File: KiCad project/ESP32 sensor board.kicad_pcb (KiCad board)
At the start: 2 copper layers, 50 parts, among them J1 USB_C_Receptacle, J3 JST_2mm_LiPo, U1 MCP73871, U2 AMS1117-3.3, U3 ESP32-C3-WROOM-02-H4, U4 CP2102N-Axx-xQFN20

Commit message: Fixed lots of bugs.
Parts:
- removed the C10 at (105.5, 117.2)
- removed the C3 at (146.6, 117.8)
- removed the C4 at (146.6, 120.8)
- removed the C6 at (146.6, 126.9)
- removed the C9 at (146.6, 132.9)
- removed the D1 at (164.0, 119.7)
- removed D10: Red, SparkFun-LED:LED_0603_1608Metric
- removed the D2 at (163.4, 134.9)
- removed the D6 at (102.5, 135.4)
- removed D7: PESD5V0S1UL_315, Footprints:DIO_PESD5V0S1UL_315
- removed the R13 at (84.0, 135.7)
- removed the R2 at (157.2, 60.3)
- removed the R9 at (166.1, 57.4)
- added C1: 0.1u, Project_Library:C_0805_2012Metric, F.Cu at (77.5, 118.5)
- added C11: 1u, Project_Library:C_0805_2012Metric, F.Cu at (66.1, 98.4)
- added C12: 10u, Project_Library:C_0805_2012Metric, F.Cu at (66.1, 107.5)
- added C13: 0.1u, Project_Library:C_0805_2012Metric, F.Cu at (66.1, 110.5)
- added C14: 0.1u, Project_Library:C_0805_2012Metric, F.Cu at (66.1, 104.5)
- added C15: 0.1u, Project_Library:C_0805_2012Metric, F.Cu at (80.2, 101.4)
- added C16: 100n, Project_Library:C_0805_2012Metric, F.Cu at (230.4, 89.2)
- added C17: 10n, Project_Library:C_0805_2012Metric, F.Cu at (230.4, 86.2)
- added C18: 100n, Project_Library:C_0805_2012Metric, F.Cu at (230.4, 77.1)
- added C19: 1u, Project_Library:C_0805_2012Metric, F.Cu at (230.4, 83.2)
- added C2: 0.1u, Project_Library:C_0805_2012Metric, F.Cu at (77.5, 121.5)
- added C20: 100n, Project_Library:C_0805_2012Metric, F.Cu at (230.4, 80.1)
- added C21: 0.1u, Project_Library:C_0805_2012Metric, F.Cu at (230.6, 104.1)
- added C22: 1u, Project_Library:C_0805_2012Metric, F.Cu at (71.0, 120.7)
- added C8: 0.1u, Project_Library:C_0805_2012Metric, F.Cu at (66.1, 101.4)
- added D4: Red, Project_Library:LED_0603_1608Metric, F.Cu at (193.4, 107.3)
- added J3: GSD090012SEU, Project_Library:AMPHENOL_GSD090012SEU, F.Cu at (206.6, 83.8)
- added J4: B4B-XH-AM__LF__SN_, Project_Library:JST_B4B-XH-AM__LF__SN_, F.Cu at (230.7, 72.0)
- added J5: B4B-XH-AM__LF__SN_, Project_Library:JST_B4B-XH-AM__LF__SN_, F.Cu at (235.3, 99.0)
- added J6: Conn_01x05, Project_Library:PinHeader_1x05_P2.54mm_Vertical, F.Cu at (226.1, 97.7)
- added MK1: CMC-5042PF-AC, Project_Library:CUI_CMC-5042PF-AC, F.Cu at (236.4, 79.4)
- added Q1: TEMT6000X01, Project_Library:TRANS_TEMT6000X01, F.Cu at (240.3, 86.0)
- added Q2: BC817, Project_Library:SOT-23, F.Cu at (66.3, 116.4)
- added Q3: BC817, Project_Library:SOT-23, F.Cu at (66.3, 121.0)
- added R17: 50, Project_Library:R_0201_0603Metric, F.Cu at (69.6, 97.8)
- added R19: 10K, Project_Library:R_0805_2012Metric, F.Cu at (203.9, 98.5)
- added R20: 50, Project_Library:R_0201_0603Metric, F.Cu at (69.6, 101.3)
- added R22: 50, Project_Library:R_0201_0603Metric, F.Cu at (69.6, 104.8)
- added R23: 10K, Project_Library:R_0201_0603Metric, F.Cu at (83.6, 101.3)
- added R24: 4K7, Project_Library:R_0201_0603Metric, F.Cu at (83.6, 97.8)
- added R25: 4K7, Project_Library:R_0201_0603Metric, F.Cu at (90.7, 99.3)
- added R26: 2K, Project_Library:R_0805_2012Metric, F.Cu at (225.9, 91.8)
- added R27: 1M, Project_Library:R_0805_2012Metric, F.Cu at (225.9, 86.0)
- added R28: 2K, Project_Library:R_0805_2012Metric, F.Cu at (225.9, 88.9)
- added R29: 1M, Project_Library:R_0805_2012Metric, F.Cu at (225.9, 83.0)
- added R30: 10K, Project_Library:R_0805_2012Metric, F.Cu at (225.9, 80.0)
- added R31: 100K, Project_Library:R_0805_2012Metric, F.Cu at (225.9, 77.1)
- added R32: 10K, Project_Library:R_0201_0603Metric, F.Cu at (70.0, 116.6)
- added R33: 10K, Project_Library:R_0201_0603Metric, F.Cu at (70.0, 114.8)
- added R34: 10K, Project_Library:R_0201_0603Metric, F.Cu at (70.0, 118.3)
- added SW1: SMD_6x3.5mm_h2.5mm, Project_Library:SW_PUSH_6mm, F.Cu at (198.9, 122.5)
- added SW2: SMD_6x3.5mm_h2.5mm, Project_Library:SW_PUSH_6mm, F.Cu at (198.9, 131.1)
- added U5: USBLC6-2SC6, Project_Library:SOT-23-6, F.Cu at (73.4, 99.3)
- added U6: W25Q32JVSSIQ, Project_Library:SOIC127P790X216-8N, F.Cu at (196.6, 100.5)
- added U7: BME280, Project_Library:PSON65P250X250X100-8N, F.Cu at (59.9, 99.1)
- added U8: MAX4466EXK, Project_Library:SOT65P210X110-5N, F.Cu at (80.1, 106.8)
- C10: renamed from C11; value 0.1 uF -> 0.1u; footprint Capacitor_SMD:C_0805_2012Metric -> Project_Library:C_0805_2012Metric
- C3: renamed from C1; value 10 uF -> 10u; footprint Capacitor_SMD:C_0805_2012Metric -> Project_Library:C_0805_2012Metric
- C4: renamed from C2; value 10 uF -> 10u; footprint Capacitor_SMD:C_0805_2012Metric -> Project_Library:C_0805_2012Metric
- C5: value 4.7 uF -> 0.1u; footprint Capacitor_SMD:C_0805_2012Metric -> Project_Library:C_0805_2012Metric
- C6: renamed from C7; value 1 uF -> 1u; footprint Capacitor_SMD:C_0805_2012Metric -> Project_Library:C_0805_2012Metric
- C7: renamed from C8; value 10 uF -> 10u; footprint Capacitor_SMD:C_0805_2012Metric -> Project_Library:C_0805_2012Metric
- C9: renamed from C12; value 4.7 uF -> 4.7u; footprint Capacitor_SMD:C_0805_2012Metric -> Project_Library:C_0805_2012Metric
- D1: renamed from D3; footprint SparkFun-LED:LED_0603_1608Metric -> Project_Library:LED_0603_1608Metric
- D2: renamed from D4; footprint SparkFun-LED:LED_0603_1608Metric -> Project_Library:LED_0603_1608Metric
- D3: renamed from D5; footprint SparkFun-LED:LED_0603_1608Metric -> Project_Library:LED_0603_1608Metric
- D5: renamed from D9; footprint SparkFun-LED:LED_0603_1608Metric -> Project_Library:LED_0603_1608Metric
- D6: renamed from D8; footprint SparkFun-LED:LED_0603_1608Metric -> Project_Library:LED_0603_1608Metric
- F1: footprint SparkFun-Fuse:1210 -> Project_Library:1210
- J1: footprint SparkFun-Connector:USB-C_16 -> Project_Library:USB-C_16
- J2: renamed from J3; footprint SparkFun-Connector:JST_SMD_2.0mm-2 -> Project_Library:JST_SMD_2.0mm-2
- R1: renamed from R7; value 10 KOhm -> 10K; footprint Resistor_SMD:R_0805_2012Metric -> Project_Library:R_0805_2012Metric
- R10: value 10 KOhm -> 330; footprint Resistor_SMD:R_0805_2012Metric -> Project_Library:R_0805_2012Metric
- R11: renamed from R18; value 1 KOhn -> 1K; footprint Resistor_SMD:R_0805_2012Metric -> Project_Library:R_0805_2012Metric
- R12: renamed from R14; value 22.1 KOhm -> 22K1; footprint Resistor_SMD:R_0805_2012Metric -> Project_Library:R_0805_2012Metric
- R13: renamed from R17; value 47.5 KOhm -> 47K5; footprint Resistor_SMD:R_0805_2012Metric -> Project_Library:R_0805_2012Metric
- R14: renamed from R20; value 330 Ohm -> 330; footprint Resistor_SMD:R_0805_2012Metric -> Project_Library:R_0805_2012Metric
- R15, R16: value 1 KOhn -> 50; footprint Resistor_SMD:R_0805_2012Metric -> Project_Library:R_0201_0603Metric
- R18: renamed from R19; value 330 Ohm -> 330; footprint Resistor_SMD:R_0805_2012Metric -> Project_Library:R_0805_2012Metric
- R2: renamed from R8; value 10 KOhm -> 10K; footprint Resistor_SMD:R_0805_2012Metric -> Project_Library:R_0805_2012Metric
- R21: value 330 Ohm -> 50; footprint Resistor_SMD:R_0805_2012Metric -> Project_Library:R_0201_0603Metric
- R3: renamed from R11; value 5.1 KOhm -> 5k1; footprint Resistor_SMD:R_0805_2012Metric -> Project_Library:R_0805_2012Metric
- R4: renamed from R12; value 5.1 KOhm -> 5K1; footprint Resistor_SMD:R_0805_2012Metric -> Project_Library:R_0805_2012Metric
- R5: renamed from R1; value 2 KOhm -> 2K; footprint Resistor_SMD:R_0805_2012Metric -> Project_Library:R_0805_2012Metric
- R6: renamed from R3; value 20 KOhm -> 20K; footprint Resistor_SMD:R_0805_2012Metric -> Project_Library:R_0805_2012Metric
- R7: renamed from R4; value 470 Ohm -> 470; footprint Resistor_SMD:R_0805_2012Metric -> Project_Library:R_0805_2012Metric
- R8: renamed from R5; value 470 Ohm -> 470; footprint Resistor_SMD:R_0805_2012Metric -> Project_Library:R_0805_2012Metric
- R9: renamed from R6; value 470 Ohm -> 470; footprint Resistor_SMD:R_0805_2012Metric -> Project_Library:R_0805_2012Metric
- U1: footprint Package_DFN_QFN:QFN-20-1EP_4x4mm_P0.5mm_EP2.5x2.5mm -> Project_Library:QFN-20-1EP_4x4mm_P0.5mm_EP2.5x2.5mm
- U2: footprint Package_TO_SOT_SMD:SOT-223-3_TabPin2 -> Project_Library:SOT-223-3_TabPin2
- U3: footprint Footprints:MODULE_ESP32-C3-WROOM-02-H4 -> Project_Library:MODULE_ESP32-C3-WROOM-02-H4
- U4: value CP2102N-Axx-xQFN20 -> CP2102N-A02-GQFN20; footprint Package_DFN_QFN:SiliconLabs_QFN-20-1EP_3x3mm_P0.5mm_EP1.8x1.8mm -> Project_Library:SiliconLabs_QFN-20-1EP_3x3mm_P0.5mm_EP1.8x1.8mm
- moved R10 100.6 mm to (81.9, 115.5)
- moved C5 69.7 mm to (77.5, 115.5)
- moved R21 40.0 mm to (69.6, 103.0)
- moved R15 37.9 mm to (69.6, 106.5)
- moved R16 33.3 mm to (69.6, 108.3)
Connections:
- C10 pad 1: VBUS -> 3.3V
- C3 pad 1: /+5V_USB -> +5V
- C5 pad 1: GND -> 3.3V
- C5 pad 2: /+5V_USB -> GND
- C9 pad 1: VBUS -> 3.3V
- F1 pad 1: Net-(D2-PadA) -> Net-(C1-Pad1)
- J1 pad A6: /D+ -> /USB_DN
- J1 pad A7: /D- -> /USB_DP
- J1 pad B6: /D+ -> /USB_DN
- J1 pad B7: /D- -> /USB_DP
- J1 pad S: unconnected-(J1-SHIELD-PadS) -> GND
- J1 pad VBUS: Net-(D2-PadC) -> Net-(C1-Pad1)
- R10 pad 1: Net-(U1-CE) -> GND
- R10 pad 2: /+5V_USB -> Net-(D4-K)
- R11 pad 1: VBUS -> 3.3V
- R12 pad 1: VBUS -> /+5V_USB
- R15 pad 1: Net-(U4-TXD) -> Net-(J3-CMD)
- R15 pad 2: Net-(U3-RXD) -> /ESP32-C3-02/MOSI_DI
- R16 pad 1: Net-(U4-RXD) -> Net-(J3-DAT0)
- R16 pad 2: Net-(U3-TXD) -> /ESP32-C3-02/MISO_DO
- R21 pad 1: GND -> /ESP32-C3-02/MOSI_DI
- U1 pad 1: /+5V_USB -> +5V
- U1 pad 17: Net-(U1-CE) -> /+5V_USB
- U1 pad 20: /+5V_USB -> +5V
- U1 pad 3: Net-(U1-SEL) -> GND
- U1 pad 4: Net-(U1-PROG2) -> /+5V_USB
- U2 pad 3: /+5V_USB -> +5V
- U3 pad 10: unconnected-(U3-IO10-Pad10) -> /ESP32-C3-02/CS
- U3 pad 11: Net-(U3-RXD) -> /ESP32-C3-02/TX_RX
- U3 pad 12: Net-(U3-TXD) -> /ESP32-C3-02/RX_TX
- U3 pad 13: unconnected-(U3-IO18-Pad13) -> /ESP32-C3-02/GPIO18
- U3 pad 14: unconnected-(U3-IO19-Pad14) -> /ESP32-C3-02/GPIO19
- U3 pad 15: unconnected-(U3-IO3-Pad15) -> /ESP32-C3-02/SCL
- U3 pad 16: unconnected-(U3-IO2-Pad16) -> /ESP32-C3-02/MISO_DO
- U3 pad 17: unconnected-(U3-IO1-Pad17) -> /ESP32-C3-02/PHOTO_C
- U3 pad 18: unconnected-(U3-IO0-Pad18) -> /ESP32-C3-02/CS_SD
- U3 pad 2: Net-(U3-EN) -> /ESP32-C3-02/EN
- U3 pad 3: unconnected-(U3-IO4-Pad3) -> /ESP32-C3-02/SDA
- U3 pad 4: unconnected-(U3-IO5-Pad4) -> /ESP32-C3-02/MIC_OUT
- U3 pad 5: unconnected-(U3-IO6-Pad5) -> /ESP32-C3-02/SCLK
- U3 pad 6: unconnected-(U3-IO7-Pad6) -> /ESP32-C3-02/MOSI_DI
- U3 pad 7: unconnected-(U3-IO8-Pad7) -> /ESP32-C3-02/GPIO8
- U3 pad 8: unconnected-(U3-IO9-Pad8) -> /ESP32-C3-02/BOOT
- U4 pad 15: unconnected-(U4-~{CTS}-Pad15) -> /ESP32-C3-02/DTS
- U4 pad 16: unconnected-(U4-~{RTS}-Pad16) -> /ESP32-C3-02/RTS
- U4 pad 17: Net-(U4-RXD) -> /ESP32-C3-02/RX_TX
- U4 pad 18: Net-(U4-TXD) -> /ESP32-C3-02/TX_RX
- U4 pad 4: /D+ -> Net-(U4-D+)
- U4 pad 5: /D- -> Net-(U4-D-)
- U4 pad 7: VBUS -> 3.3V

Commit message: Configured the layout editor.
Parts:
- C1, C10, C11, C12, C13, C14, C15, C16, C17, C18, C19, C2, C20, C21, C22, C3, C4, C5, C6, C7, C8, C9: footprint Project_Library:C_0805_2012Metric -> Capacitor_SMD:C_0805_2012Metric
- D1, D2, D3, D4, D5, D6: footprint Project_Library:LED_0603_1608Metric -> LED_SMD:LED_0603_1608Metric
- J6: footprint Project_Library:PinHeader_1x05_P2.54mm_Vertical -> Connector_PinHeader_2.54mm:PinHeader_1x05_P2.54mm_Vertical
- Q2, Q3: footprint Project_Library:SOT-23 -> Package_TO_SOT_SMD:SOT-23
- R1, R10, R11, R12, R13, R14, R18, R19, R2, R26, R27, R28, R29, R3, R30, R31, R4, R5, R6, R7, R8, R9: footprint Project_Library:R_0805_2012Metric -> Resistor_SMD:R_0805_2012Metric
- R15, R16, R17, R20, R21, R22, R23, R24, R25, R32, R33, R34: footprint Project_Library:R_0201_0603Metric -> Resistor_SMD:R_0805_2012Metric
- SW1, SW2: footprint Project_Library:SW_PUSH_6mm -> Button_Switch_THT:SW_PUSH_6mm
- U1: footprint Project_Library:QFN-20-1EP_4x4mm_P0.5mm_EP2.5x2.5mm -> Package_DFN_QFN:QFN-20-1EP_4x4mm_P0.5mm_EP2.5x2.5mm
- U2: footprint Project_Library:SOT-223-3_TabPin2 -> Package_TO_SOT_SMD:SOT-223-3_TabPin2
- U4: footprint Project_Library:SiliconLabs_QFN-20-1EP_3x3mm_P0.5mm_EP1.8x1.8mm -> Package_DFN_QFN:SiliconLabs_QFN-20-1EP_3x3mm_P0.5mm_EP1.8x1.8mm
- U5: footprint Project_Library:SOT-23-6 -> Package_TO_SOT_SMD:SOT-23-6

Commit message: Completed draft layout.
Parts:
- removed J4: B4B-XH-AM__LF__SN_, Project_Library:JST_B4B-XH-AM__LF__SN_
- removed R4: 5K1, Resistor_SMD:R_0805_2012Metric
- moved Q3 123.4 mm to (184.0, 83.8)
- moved R32 121.4 mm to (191.2, 110.8)
- moved C22 120.6 mm to (191.5, 115.2), turned to 180 degrees
- moved Q2 118.3 mm to (184.5, 111.0)
- moved Q1 115.7 mm to (125.0, 76.2)
- moved R34 114.1 mm to (178.5, 83.0)
- moved C8 112.5 mm to (178.2, 92.5)
- moved R20 108.8 mm to (178.2, 97.2)
- moved R21 108.7 mm to (178.2, 101.0)
- moved R22 108.7 mm to (178.2, 104.8)
- moved R33 108.1 mm to (178.0, 109.5)
- moved C14 103.8 mm to (169.0, 90.5), turned to 180 degrees
- moved D4 99.7 mm to (94.2, 118.0), turned to 180 degrees
- moved U3 88.3 mm to (192.7, 96.6), turned to -90 degrees
- moved R8 84.8 mm to (99.2, 114.8), turned to 180 degrees
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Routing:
- net /USB_DN: track 0.00 -> 3.54 mm
- net /USB_DP: track 0.00 -> 3.33 mm
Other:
- copper layers 2 -> 4

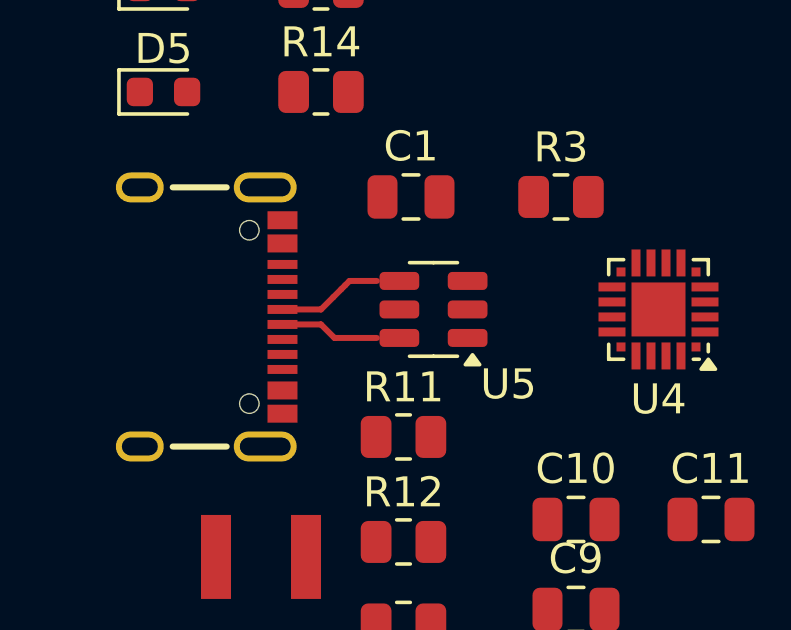
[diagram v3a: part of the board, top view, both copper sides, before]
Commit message: Experimenting with lenght tuning of the USB data tracks.
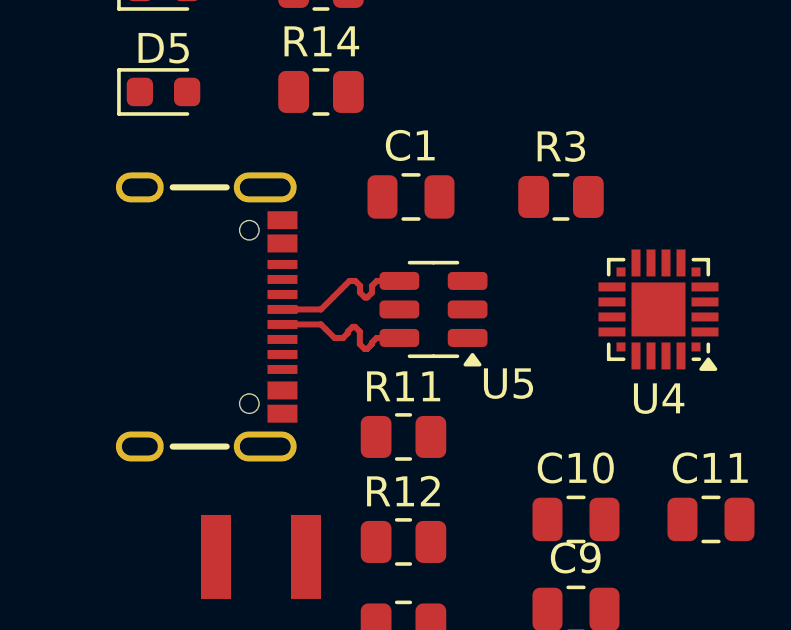
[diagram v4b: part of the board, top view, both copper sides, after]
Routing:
- net /USB_DP: track 3.33 -> 5.00 mm
- net /USB_DN: track 3.54 -> 5.01 mm

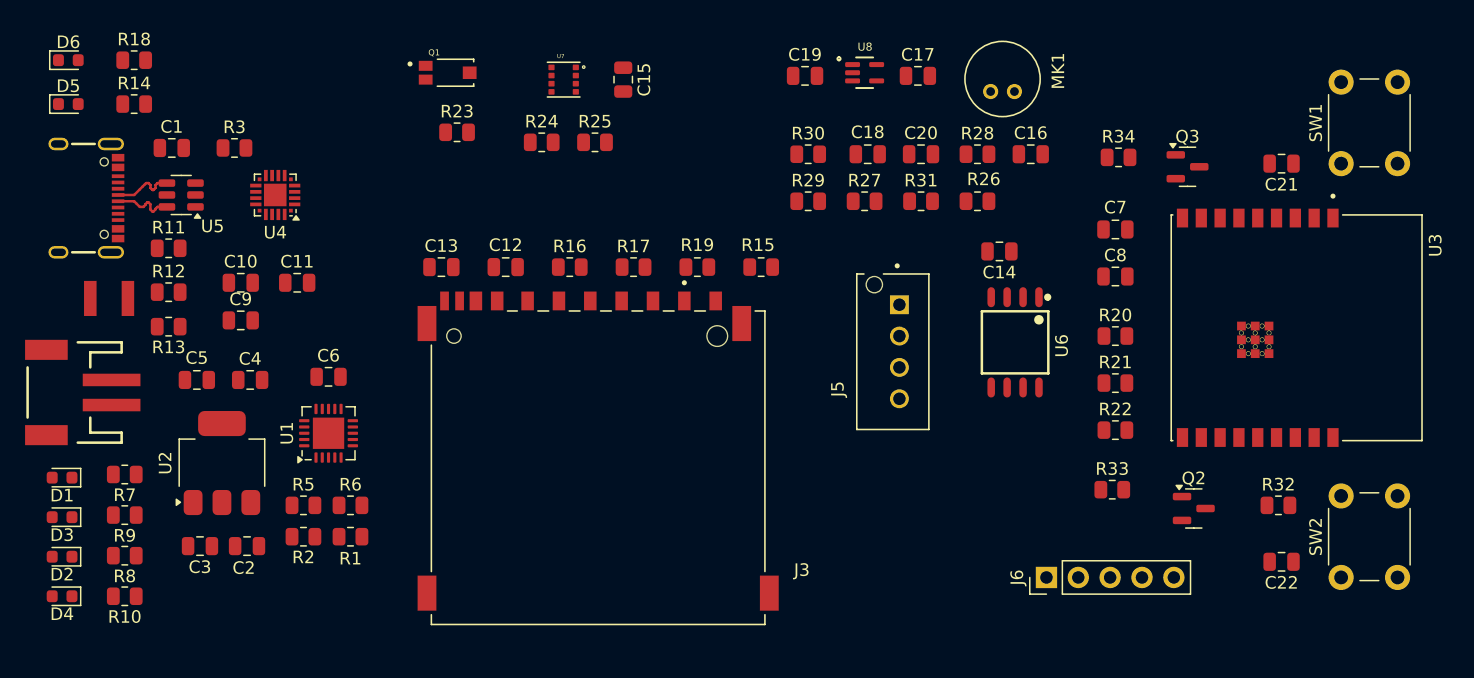
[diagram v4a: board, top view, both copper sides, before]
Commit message: Autorouting experiment. Layout is incomplete.
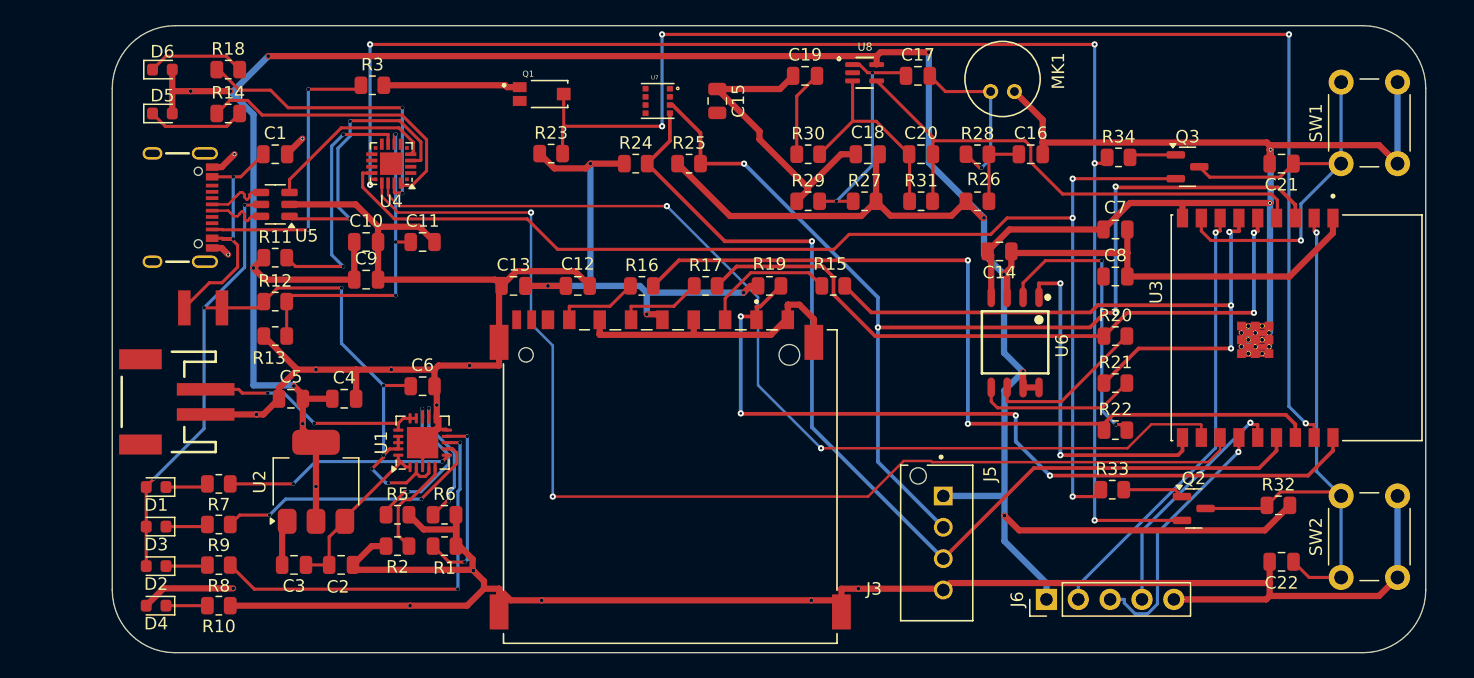
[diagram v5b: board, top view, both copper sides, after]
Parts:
- moved J5 15.6 mm to (164.0, 113.8)
- moved R3 12.1 mm to (119.0, 77.2)
- moved C10 10.5 mm to (118.5, 89.8)
- moved C11 10.5 mm to (123.0, 89.8)
- moved C9 10.5 mm to (118.5, 92.8)
- moved U4 9.58 mm to (120.5, 83.5)
- moved R11 8.53 mm to (111.2, 91.0)
- moved R12 8.53 mm to (111.2, 94.5)
- moved R13 8.53 mm to (111.2, 97.2)
- moved C1 8.27 mm to (111.2, 82.8)
- moved C15 7.69 mm to (146.5, 78.5)
- moved Q1 7.69 mm to (132.5, 78.0)
- moved R23 7.69 mm to (133.2, 82.7)
- moved R24 7.69 mm to (140.0, 83.5)
- moved R25 7.69 mm to (144.2, 83.5)
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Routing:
- net GND: track 0.00 -> 391.3 mm, vias 0 -> 15
- net 3.3V: track 0.00 -> 316.2 mm, vias 0 -> 17
- net /ESP32-C3-02/RTS: track 0.00 -> 116.0 mm, vias 0 -> 5
- net /ESP32-C3-02/PHOTO_C: track 0.00 -> 103.3 mm, vias 0 -> 4
- net /ESP32-C3-02/DTS: track 0.00 -> 97.6 mm, vias 0 -> 3
- net /ESP32-C3-02/RX_TX: track 0.00 -> 92.7 mm, vias 0 -> 2
- net /ESP32-C3-02/SDA: track 0.00 -> 90.4 mm, vias 0 -> 4
- net /ESP32-C3-02/SCL: track 0.00 -> 81.3 mm, vias 0 -> 1
- net /ESP32-C3-02/TX_RX: track 0.00 -> 80.1 mm, vias 0 -> 2
- net /+5V_USB: track 0.00 -> 72.3 mm, vias 0 -> 8
- net /ESP32-C3-02/MISO_DO: track 0.00 -> 67.2 mm, vias 0 -> 2
- net /ESP32-C3-02/CS_SD: track 0.00 -> 65.0 mm, vias 0 -> 4
- net /ESP32-C3-02/SCLK: track 0.00 -> 55.1 mm, vias 0 -> 2
- net /ESP32-C3-02/MOSI_DI: track 0.00 -> 54.4 mm, vias 0 -> 3
- net /ESP32-C3-02/EN: track 0.00 -> 45.4 mm, vias 0 -> 1
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- added copper zone on In2.Cu, net 3.3V
- added copper zone on In1.Cu, net GND
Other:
- board outline added: 104.8 x 50 mm

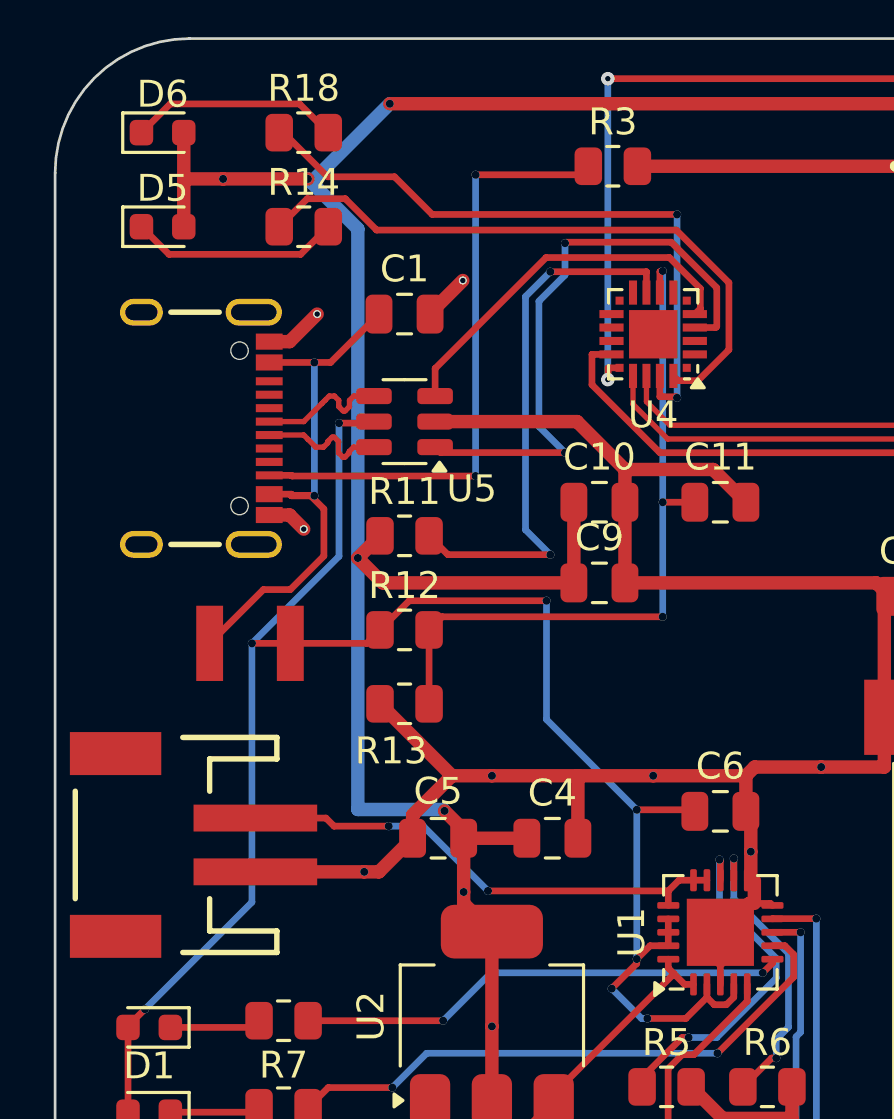
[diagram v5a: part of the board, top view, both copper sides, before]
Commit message: Trying routing, layout, and changed USB and battery connectors.
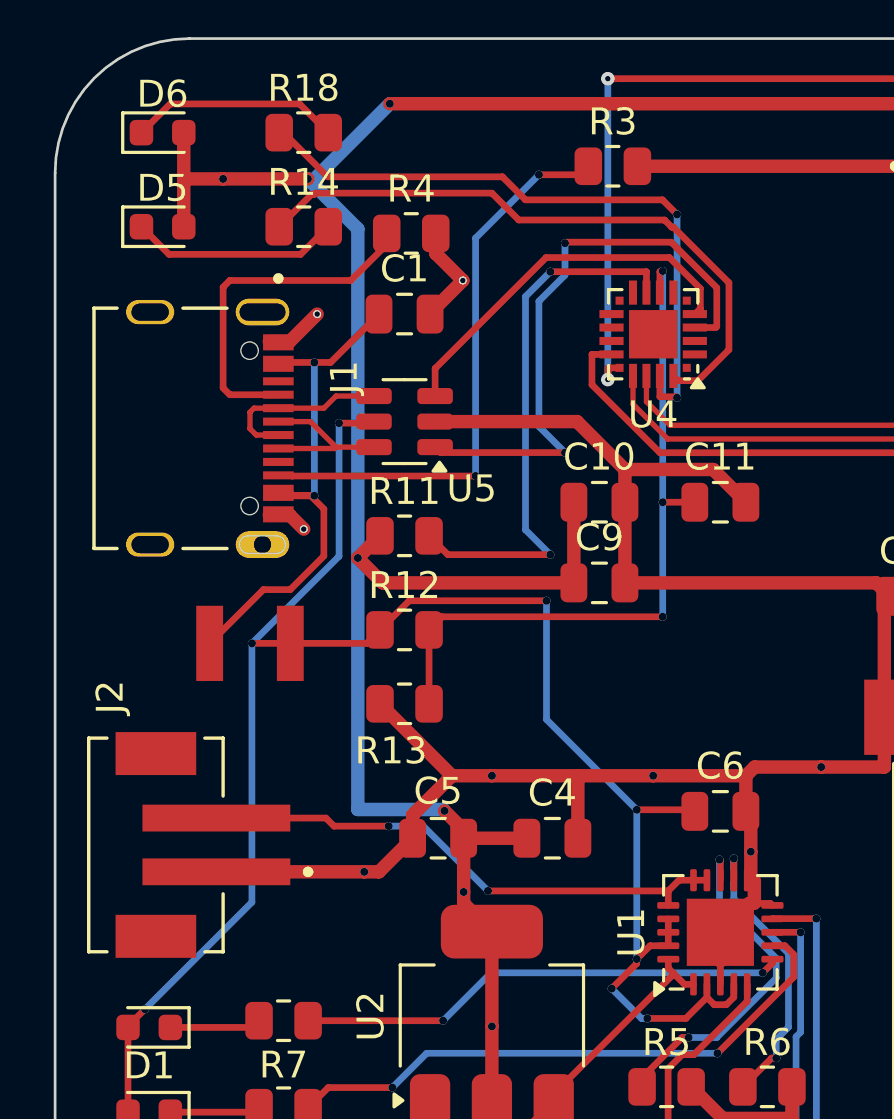
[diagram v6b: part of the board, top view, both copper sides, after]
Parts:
- added R4: 5K1, Resistor_SMD:R_0805_2012Metric, F.Cu at (111.5, 79.8)
- J1: footprint Project_Library:USB-C_16 -> Footprints:VALCON_CSP-USC16-TR
- J2: footprint Project_Library:JST_SMD_2.0mm-2 -> Footprints:JST_B2B-PH-SM4-TB
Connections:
- net Net-(U4-D+) renamed /ESP32-C3-02/USB_D+
- net Net-(U4-D-) renamed /ESP32-C3-02/USB_D-
- C1 pad 1: Net-(C1-Pad1) -> /VBUS
- F1 pad 1: Net-(C1-Pad1) -> /VBUS
- J1 pad A6: /USB_DN -> /USB_DP
- J1 pad A7: /USB_DP -> /USB_DN
- J1 pad B6: /USB_DN -> /USB_DP
- J1 pad B7: /USB_DP -> /USB_DN
- J2 pad 1: GND -> /VBAT
- J2 pad 2: /VBAT -> GND
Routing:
- net Net-(C1-Pad1): track 20.3 -> 0.00 mm, vias 2 -> 0
- net /VBUS: track 0.00 -> 20.3 mm, vias 0 -> 2
- net Net-(J1-CC1): track 0.00 -> 12.7 mm
- net GND: track 391.3 -> 393.4 mm
- net /USB_DN: track 5.02 -> 6.63 mm
- net Net-(J1-CC2): track 23.2 -> 21.8 mm
- net /USB_DP: track 5.00 -> 6.11 mm
